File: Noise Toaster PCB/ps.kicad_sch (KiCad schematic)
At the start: 8 parts

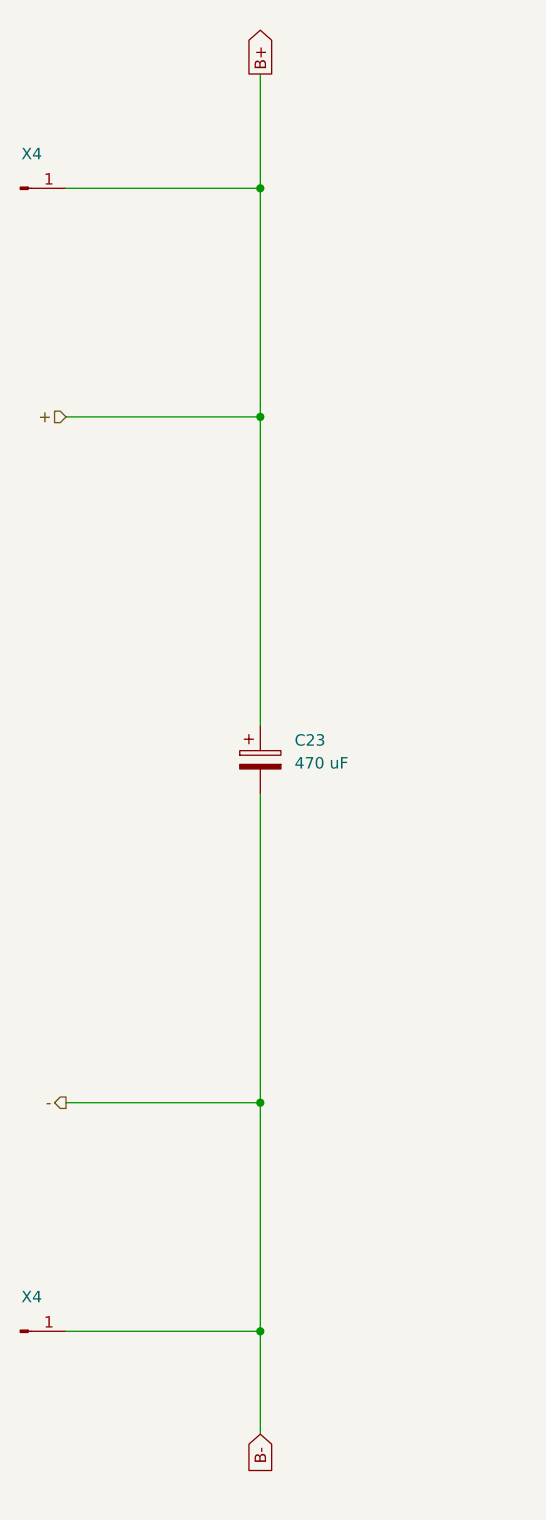
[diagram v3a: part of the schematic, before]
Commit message: applied footprints
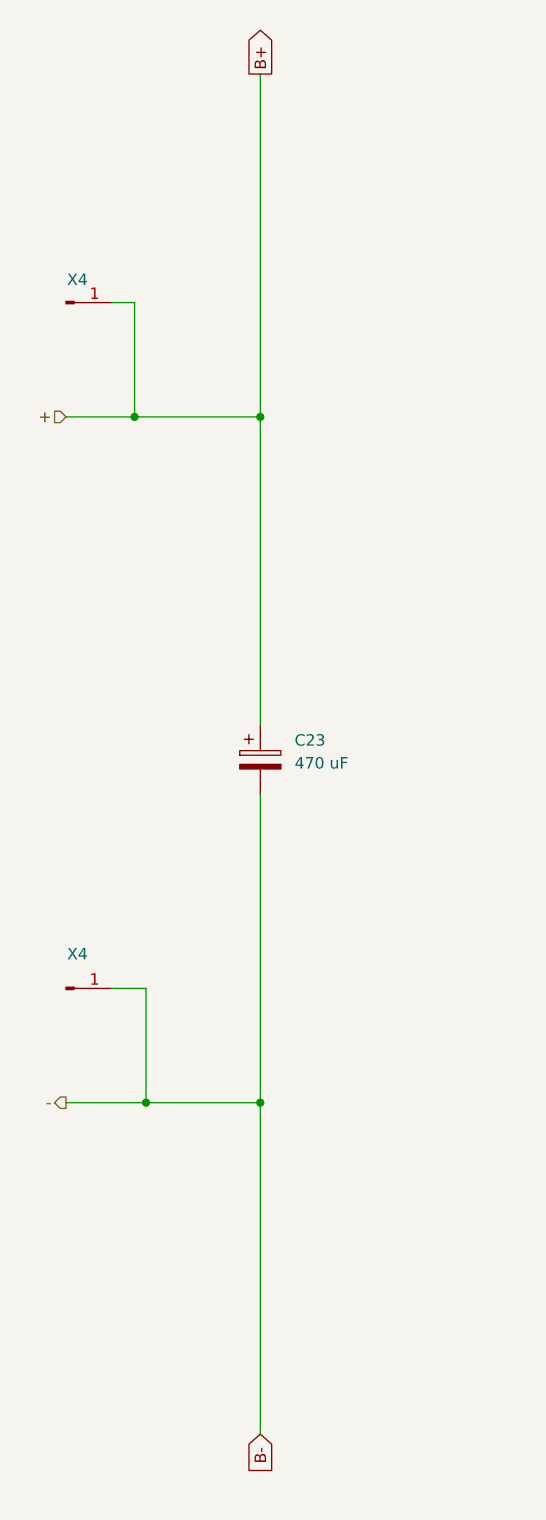
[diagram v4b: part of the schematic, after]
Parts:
- removed X4 (x2): ~, symbol Connector:Conn_01x01_Pin
- added X4 (x2): ~, Connector_PinHeader_1.00mm:PinHeader_1x01_P1.00mm_Vertical, symbol Connector:Conn_01x01_Pin
- C13, C14: footprint (none) -> Capacitor_THT:CP_Radial_D4.0mm_P1.50mm
- C15, C23: footprint (none) -> Capacitor_THT:CP_Radial_D14.0mm_P5.00mm
- R37, R42: footprint (none) -> Resistor_THT:R_Axial_DIN0207_L6.3mm_D2.5mm_P10.16mm_Horizontal
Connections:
- net B+: now also X4.1 (Pin_1)
- net B-: now also X4.1 (Pin_1)
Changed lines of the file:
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@@
   (junction (at 59.69 139.7) (diameter 0) (color 0 0 0 0)
   )
-  (junction (at 59.69 165.1) (diameter 0) (color 0 0 0 0)
+  (junction (at 45.72 63.5) (diameter 0) (color 0 0 0 0)
+  )
+  (junction (at 46.99 139.7) (diameter 0) (color 0 0 0 0)
   )
   (junction (at 160.02 105.41) (diameter 0) (color 0 0 0 0)
@@
   (junction (at 59.69 63.5) (diameter 0) (color 0 0 0 0)
   )
-  (junction (at 59.69 38.1) (diameter 0) (color 0 0 0 0)
-  )
   (junction (at 105.41 104.14) (diameter 0) (color 0 0 0 0)
   )
-  (wire (pts (xy 38.1 139.7) (xy 59.69 139.7))
-    (stroke (width 0) (type default))
-  )
-  (wire (pts (xy 59.69 38.1) (xy 59.69 63.5))
+  (wire (pts (xy 38.1 139.7) (xy 46.99 139.7))
+    (stroke (width 0) (type default))
+  )
+  (wire (pts (xy 59.69 25.4) (xy 59.69 63.5))
     (stroke (width 0) (type default))
   )
@@
     (stroke (width 0) (type default))
   )
-  (wire (pts (xy 38.1 38.1) (xy 59.69 38.1))
+  (wire (pts (xy 46.99 127) (xy 46.99 139.7))
+    (stroke (width 0) (type default))
+  )
+  (wire (pts (xy 46.99 139.7) (xy 59.69 139.7))
     (stroke (width 0) (type default))
   )
@@
     (stroke (width 0) (type default))
   )
+  (wire (pts (xy 43.18 127) (xy 46.99 127))
+    (stroke (width 0) (type default))
+  )
   (wire (pts (xy 160.02 105.41) (xy 160.02 133.35))
     (stroke (width 0) (type default))
   )
-  (wire (pts (xy 38.1 63.5) (xy 59.69 63.5))
+  (wire (pts (xy 38.1 63.5) (xy 45.72 63.5))
     (stroke (width 0) (type default))
   )
@@
     (stroke (width 0) (type default))
   )
+  (wire (pts (xy 45.72 50.8) (xy 45.72 63.5))
+    (stroke (width 0) (type default))
+  )
   (wire (pts (xy 160.02 105.41) (xy 224.79 105.41))
     (stroke (width 0) (type default))
@@
     (stroke (width 0) (type default))
   )
-  (wire (pts (xy 59.69 165.1) (xy 59.69 176.53))
+  (wire (pts (xy 43.18 50.8) (xy 45.72 50.8))
+    (stroke (width 0) (type default))
+  )
+  (wire (pts (xy 59.69 139.7) (xy 59.69 176.53))
     (stroke (width 0) (type default))
   )
@@
     (stroke (width 0) (type default))
   )
-  (wire (pts (xy 59.69 139.7) (xy 59.69 165.1))
+  (wire (pts (xy 45.72 63.5) (xy 59.69 63.5))
     (stroke (width 0) (type default))
   )
@@
   )
   (wire (pts (xy 160.02 63.5) (xy 160.02 105.41))
-    (stroke (width 0) (type default))
-  )
-  (wire (pts (xy 38.1 165.1) (xy 59.69 165.1))
-    (stroke (width 0) (type default))
-  )
-  (wire (pts (xy 59.69 25.4) (xy 59.69 38.1))
     (stroke (width 0) (type default))
   )
@@
     (effects (font (size 1.27 1.27)) (justify right))
   )
-  (symbol (lib_id "Connector:Conn_01x01_Pin") (at 33.02 38.1 0) (unit 1)
+  (symbol (lib_id "Connector:Conn_01x01_Pin") (at 38.1 127 0) (unit 1)
     (in_bom yes) (on_board yes) (dnp no)
-    (property "Reference" "X4" (at 34.29 34.29 0)
-      (effects (font (size 1.27 1.27)))
-    )
-    (property "Value" "~" (at 33.655 35.56 0)
-      (effects (font (size 1.27 1.27)))
-    )
-    (property "Footprint" "" (at 33.02 38.1 0)
-      (effects (font (size 1.27 1.27)) hide)
-    )
-    (property "Datasheet" "~" (at 33.02 38.1 0)
+    (property "Reference" "X4" (at 39.37 123.19 0)
+      (effects (font (size 1.27 1.27)))
+    )
+    (property "Value" "~" (at 38.735 124.46 0)
+      (effects (font (size 1.27 1.27)))
+    )
+    (property "Footprint" "Connector_PinHeader_1.00mm:PinHeader_1x01_P1.00mm_Vertical" (at 38.1 127 0)
+      (effects (font (size 1.27 1.27)) hide)
+    )
+    (property "Datasheet" "~" (at 38.1 127 0)
       (effects (font (size 1.27 1.27)) hide)
     )
@@
         )
         (path "/7be3f398-d902-4566-9ee4-0bff072cd47e/d0369b76-3398-4137-86ba-22490a5aca99"
-          (reference "X21") (unit 1)
+          (reference "X22") (unit 1)
         )
         (path "/7be3f398-d902-4566-9ee4-0bff072cd47e/0647ade8-e724-4924-aa52-6cbb42374298"
-          (reference "X21") (unit 1)
-        )
-        (path "/7be3f398-d902-4566-9ee4-0bff072cd47e/8163954c-0389-42ef-b929-449d078595e3"
-          (reference "B+") (unit 1)
-        )
-      )
-    )
-  )
-  (symbol (lib_id "Connector:Conn_01x01_Pin") (at 33.02 165.1 0) (unit 1)
+          (reference "X22") (unit 1)
+        )
+        (path "/7be3f398-d902-4566-9ee4-0bff072cd47e/8163954c-0389-42ef-b929-449d078595e3"
+          (reference "X-1") (unit 1)
+        )
+      )
+    )
+  )
+  (symbol (lib_id "Connector:Conn_01x01_Pin") (at 38.1 50.8 0) (unit 1)
     (in_bom yes) (on_board yes) (dnp no)
-    (property "Reference" "X4" (at 34.29 161.29 0)
-      (effects (font (size 1.27 1.27)))
-    )
-    (property "Value" "~" (at 33.655 162.56 0)
-      (effects (font (size 1.27 1.27)))
-    )
-    (property "Footprint" "" (at 33.02 165.1 0)
-      (effects (font (size 1.27 1.27)) hide)
-    )
-    (property "Datasheet" "~" (at 33.02 165.1 0)
+    (property "Reference" "X4" (at 39.37 48.26 0)
+      (effects (font (size 1.27 1.27)))
+    )
+    (property "Value" "~" (at 38.735 48.26 0)
+      (effects (font (size 1.27 1.27)))
+    )
+    (property "Footprint" "Connector_PinHeader_1.00mm:PinHeader_1x01_P1.00mm_Vertical" (at 38.1 50.8 0)
+      (effects (font (size 1.27 1.27)) hide)
+    )
+    (property "Datasheet" "~" (at 38.1 50.8 0)
       (effects (font (size 1.27 1.27)) hide)
     )
@@
         )
         (path "/7be3f398-d902-4566-9ee4-0bff072cd47e/d0369b76-3398-4137-86ba-22490a5aca99"
-          (reference "X21") (unit 1)
+          (reference "X22") (unit 1)
         )
         (path "/7be3f398-d902-4566-9ee4-0bff072cd47e/0647ade8-e724-4924-aa52-6cbb42374298"
-          (reference "X21") (unit 1)
-        )
-        (path "/7be3f398-d902-4566-9ee4-0bff072cd47e/8163954c-0389-42ef-b929-449d078595e3"
-          (reference "B-") (unit 1)
+          (reference "X22") (unit 1)
+        )
+        (path "/7be3f398-d902-4566-9ee4-0bff072cd47e/8163954c-0389-42ef-b929-449d078595e3"
+          (reference "X+1") (unit 1)
         )
       )
@@
       (effects (font (size 1.27 1.27)) (justify left))
     )
-    (property "Footprint" "" (at 60.6552 105.41 0)
+    (property "Footprint" "Capacitor_THT:CP_Radial_D14.0mm_P5.00mm" (at 60.6552 105.41 0)
       (effects (font (size 1.27 1.27)) hide)
     )
@@
       (effects (font (size 1.27 1.27)) (justify left))
     )
-    (property "Footprint" "" (at 160.9852 140.97 0)
+    (property "Footprint" "Capacitor_THT:CP_Radial_D14.0mm_P5.00mm" (at 160.9852 140.97 0)
       (effects (font (size 1.27 1.27)) hide)
     )
@@
       (effects (font (size 1.27 1.27)) (justify left))
     )
-    (property "Footprint" "" (at 223.012 120.65 90)
+    (property "Footprint" "Resistor_THT:R_Axial_DIN0207_L6.3mm_D2.5mm_P10.16mm_Horizontal" (at 223.012 120.65 90)
       (effects (font (size 1.27 1.27)) hide)
     )
@@
       (effects (font (size 1.27 1.27)) (justify left))
     )
-    (property "Footprint" "" (at 106.3752 83.82 0)
+    (property "Footprint" "Capacitor_THT:CP_Radial_D4.0mm_P1.50mm" (at 106.3752 83.82 0)
       (effects (font (size 1.27 1.27)) hide)
     )
@@
       (effects (font (size 1.27 1.27)) (justify left))
     )
-    (property "Footprint" "" (at 158.242 45.72 90)
+    (property "Footprint" "Resistor_THT:R_Axial_DIN0207_L6.3mm_D2.5mm_P10.16mm_Horizontal" (at 158.242 45.72 90)
       (effects (font (size 1.27 1.27)) hide)
     )
@@
       (effects (font (size 1.27 1.27)) (justify left))
     )
-    (property "Footprint" "" (at 106.3752 133.35 0)
-      (effects (font (size 1.27 1.27)) hide)
-    )
+    (property "Footprint" "Capacitor_THT:CP_Radial_D4.0mm_P1.50mm" (at 106.3752 133.35 0)
+      (effects (font (size 1.27 1.27)) hide)
+    )

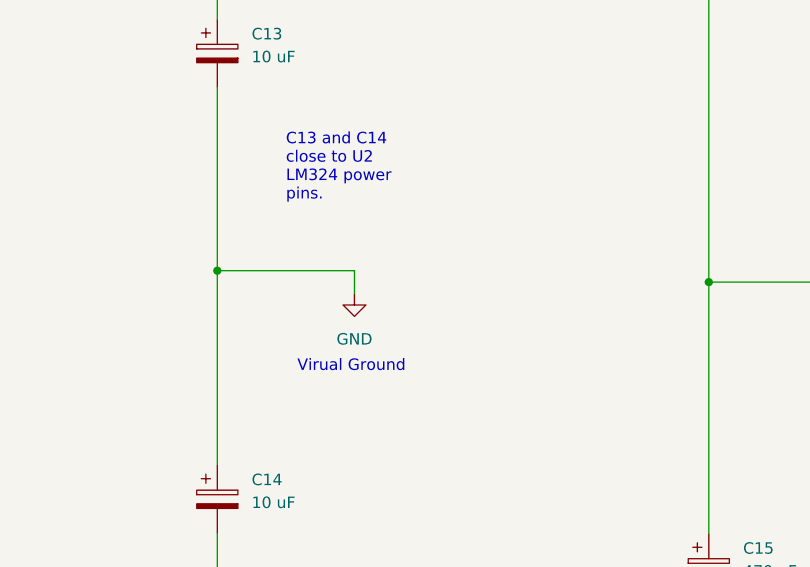
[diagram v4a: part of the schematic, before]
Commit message: placed pards of the pcb properly
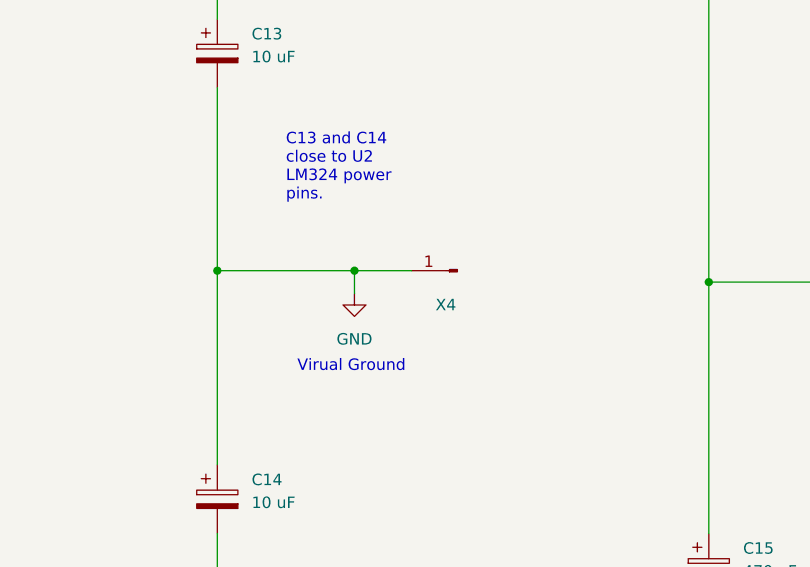
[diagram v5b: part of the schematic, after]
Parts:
- added X4: ~, Connector_PinHeader_1.00mm:PinHeader_1x01_P1.00mm_Vertical, symbol Connector:Conn_01x01_Pin
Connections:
- net GND: now also X4.1 (Pin_1)
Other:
- company: http://musicfromouterspace.com/analogsynth_new/NOISETOASTER/NOISETOASTER.php -> Music From Outer Space LLC
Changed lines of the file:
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@@
     (title "Power Supply")
     (rev "0.5")
-    (company "http://musicfromouterspace.com/analogsynth_new/NOISETOASTER/NOISETOASTER.php")
+    (company "Music From Outer Space LLC")
     (comment 1 "Licence: CC-BY-NC-SA")
     (comment 2 "Original Design by Ray Wilson")
-    (comment 3 "Music From Outer Space LLC")
+    (comment 3 "http://musicfromouterspace.com/analogsynth_new/NOISETOASTER/NOISETOASTER.php")
+  )
+  (junction (at 120.65 104.14) (diameter 0) (color 0 0 0 0)
   )
   (junction (at 59.69 139.7) (diameter 0) (color 0 0 0 0)
@@
   )
   (wire (pts (xy 59.69 105.41) (xy 59.69 139.7))
+    (stroke (width 0) (type default))
+  )
+  (wire (pts (xy 120.65 104.14) (xy 127 104.14))
     (stroke (width 0) (type default))
   )
@@
         )
       )
+    )
+  )
+  (symbol (lib_id "Connector:Conn_01x01_Pin") (at 132.08 104.14 180) (unit 1)
+    (in_bom yes) (on_board yes) (dnp no)
+    (property "Reference" "X4" (at 130.81 107.95 0)
+      (effects (font (size 1.27 1.27)))
+    )
+    (property "Value" "~" (at 131.445 106.68 0)
+      (effects (font (size 1.27 1.27)))
+    )
+    (property "Footprint" "Connector_PinHeader_1.00mm:PinHeader_1x01_P1.00mm_Vertical" (at 132.08 104.14 0)
+      (effects (font (size 1.27 1.27)) hide)
+    )
+    (property "Datasheet" "~" (at 132.08 104.14 0)
+      (effects (font (size 1.27 1.27)) hide)
+    )
+    (pin "1")
+    (instances
+      (project "Noise Toaster PCB"
+        (path "/7be3f398-d902-4566-9ee4-0bff072cd47e/818b46cb-815d-4132-b52d-9731333b7f1f"
+          (reference "X4") (unit 1)
+        )
+        (path "/7be3f398-d902-4566-9ee4-0bff072cd47e/d0369b76-3398-4137-86ba-22490a5aca99"
+          (reference "X22") (unit 1)
+        )
+        (path "/7be3f398-d902-4566-9ee4-0bff072cd47e/0647ade8-e724-4924-aa52-6cbb42374298"
+          (reference "X22") (unit 1)
+        )
+        (path "/7be3f398-d902-4566-9ee4-0bff072cd47e/8163954c-0389-42ef-b929-449d078595e3"
+          (reference "GND1") (unit 1)
+        )
+      )
